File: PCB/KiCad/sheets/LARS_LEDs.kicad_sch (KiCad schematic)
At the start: 27 parts, among them J30 LED1, J31 LED2, SW2 User Button

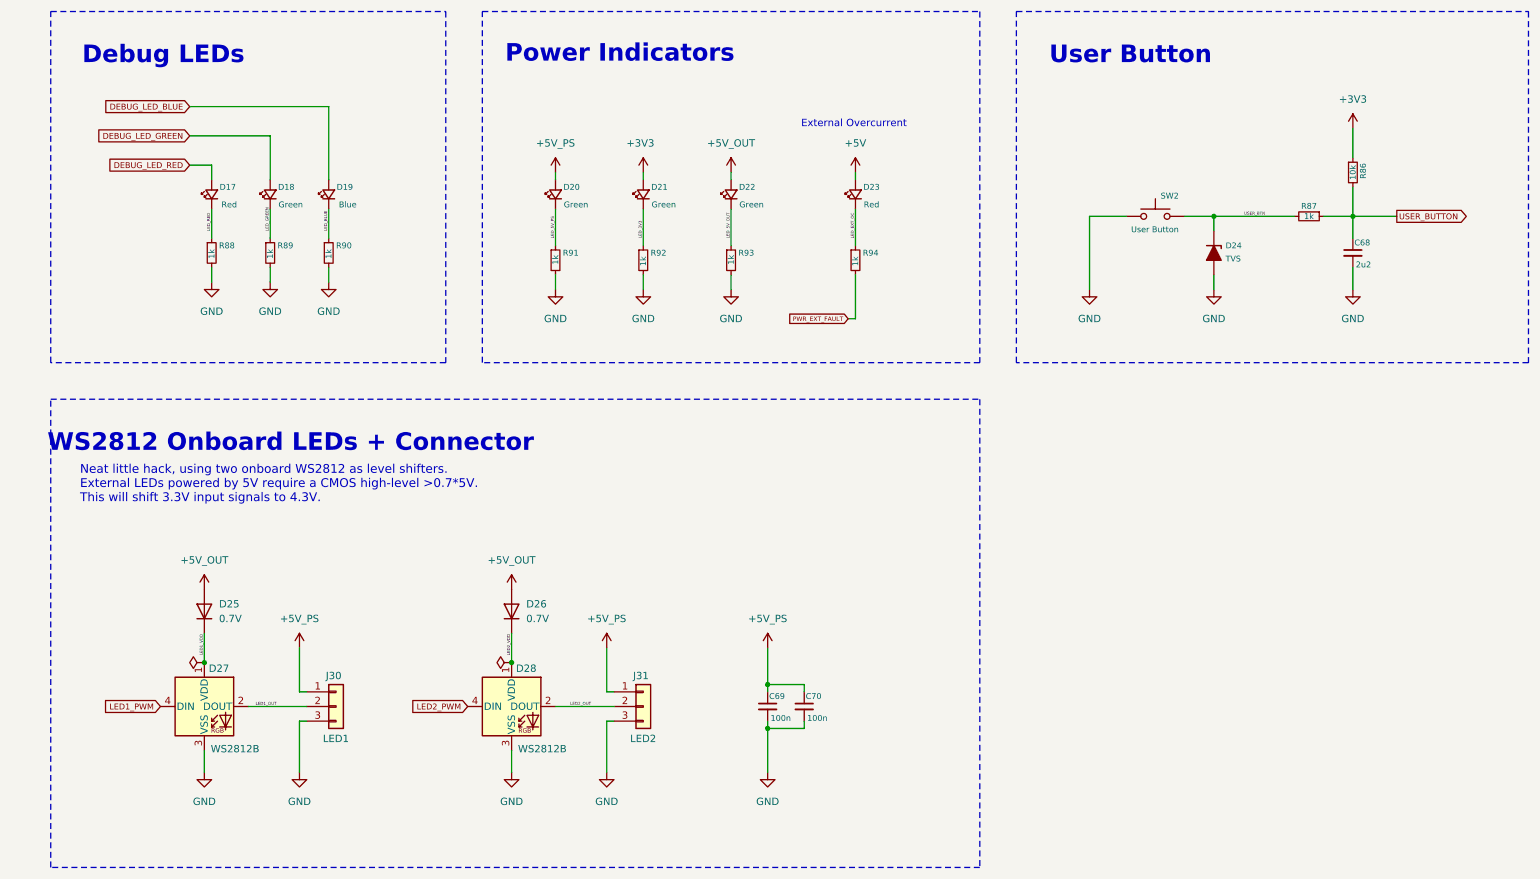
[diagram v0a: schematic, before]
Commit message: PCB: add XOR gate for RC Receiver
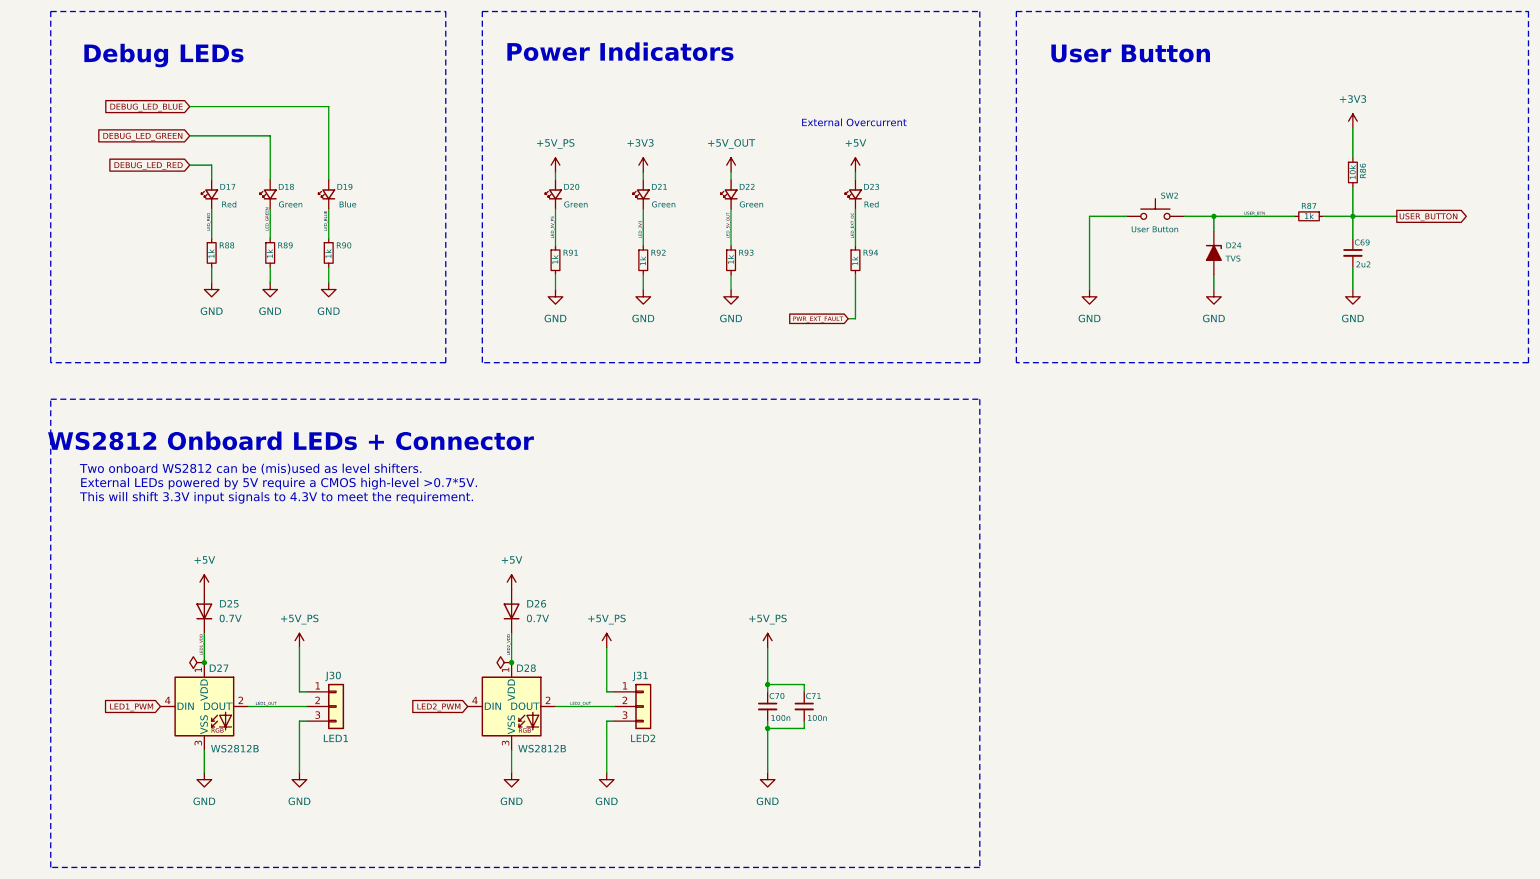
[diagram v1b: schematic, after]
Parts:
- renumbered C68 to C69, C69 to C70, C70 to C71
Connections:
- net +5V: now also D25.2 (A), D26.2 (A)
- net +5V_OUT: no longer D25.2 (A), D26.2 (A)
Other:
- note added: "Two onboard WS2812 can be (mis)used as level shifters. External LEDs powered by 5V require a CMOS high-level >0.7*5V. This will shift 3.3V input signals to 4.3V to meet the requirement."
- note removed: "Neat little hack, using two onboard WS2812 as level shifters. External LEDs powered by 5V require a CMOS high-level >0.7*5V. This will shift 3.3V input signals to 4.3V."
